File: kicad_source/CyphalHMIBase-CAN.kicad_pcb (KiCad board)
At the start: 2 copper layers, 52 x 36 mm, 62 parts, among them CN1 RASPBERRYPI_PICO, CN12 S3B-PH-SM4-TB, CN2 SM04B-SRSS-TB, CN3 SM04B-SRSS-TB, CN4 SM04B-GHS-TB, CN5 SM04B-GHS-TB, CN7 DNI, CN8 DNI, SW1 PTS636 SM43 SMTR LFS, U3 M24C64-RMN6TP, U8 MCP2515T-I/SO, U9 SN65HVD230, Y1 X322516MLB4SI

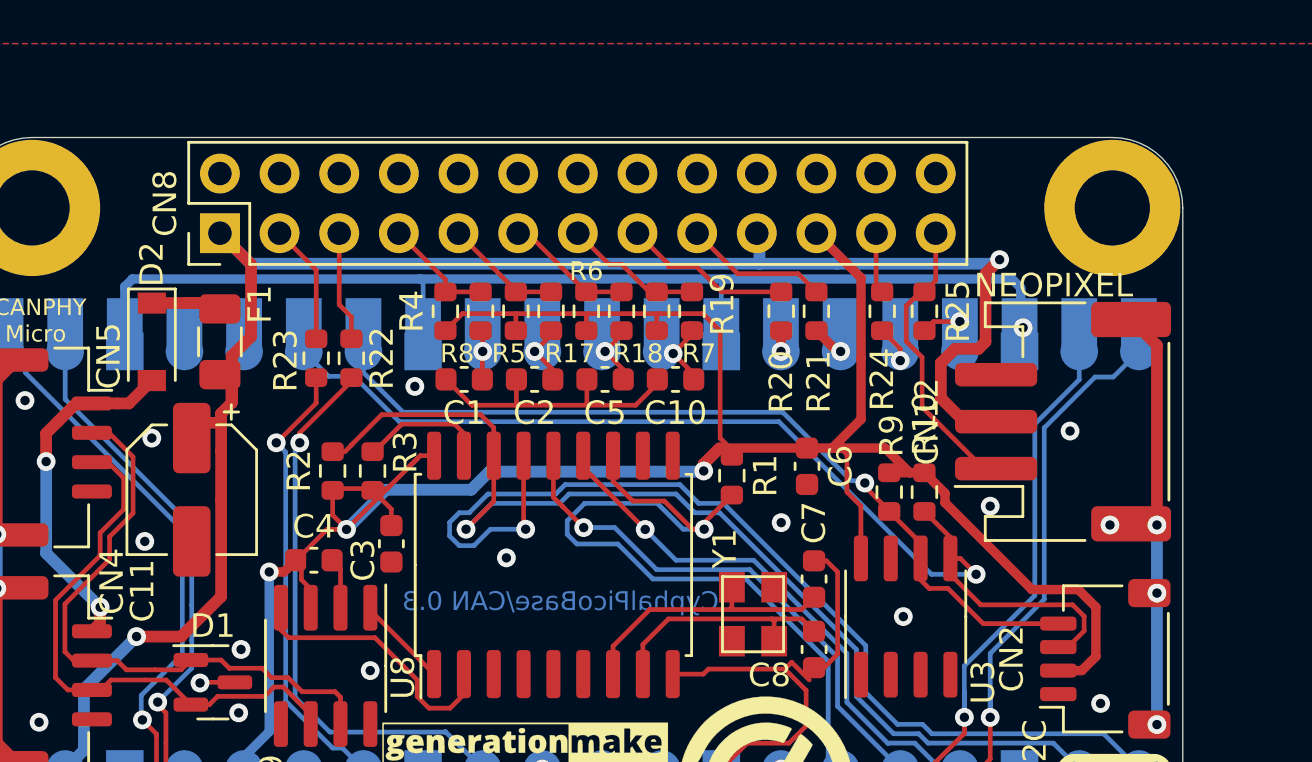
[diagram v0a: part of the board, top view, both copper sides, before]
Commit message: removed unnecessary parts
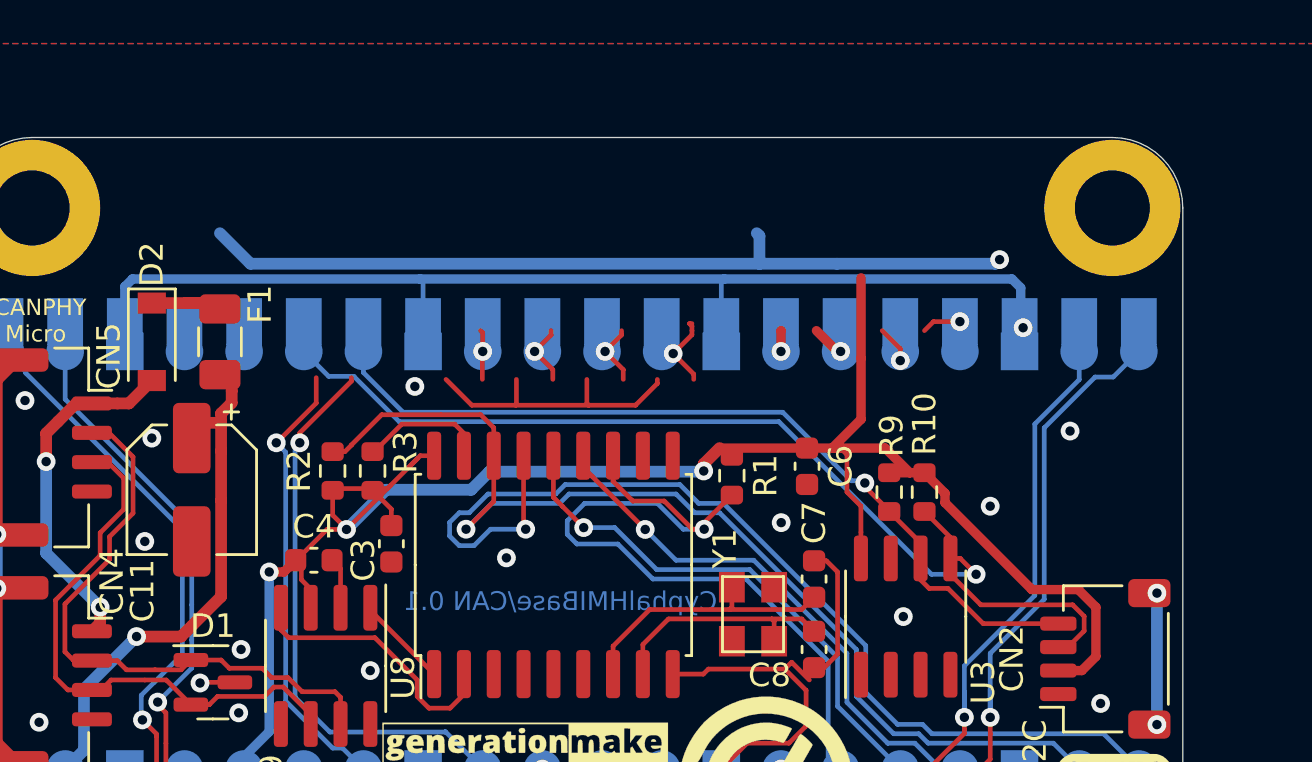
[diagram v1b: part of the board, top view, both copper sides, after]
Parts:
- removed C1, C10, C2, C5: 100nF, Capacitor_SMD:C_0603_1608Metric
- removed CN12: S3B-PH-SM4-TB, generationmake:JST_PH_S3B-PH-SM4-TB_1x03-1MP_P2.00mm_Horizontal
- removed CN8: DNI, Connector_PinHeader_2.54mm:PinHeader_2x13_P2.54mm_Vertical
- removed R17, R18, R19, R4, R5, R6, R7, R8: 10k, Resistor_SMD:R_0603_1608Metric
- removed R20, R21, R22, R23, R24, R25: 100R, Resistor_SMD:R_0603_1608Metric
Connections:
- CN1 pad 10: /INPUT1 -> /TFT_DC
- CN1 pad 11: /INPUT2 -> unconnected-(CN1-GP8/SPI1_RX/I2C0_SDA/UART1_TX-Pad11)
- CN1 pad 12: /INPUT3 -> /TFT_RST
- CN1 pad 14: /OUTPUT0 -> /SPI1_CLK
- CN1 pad 15: /OUTPUT1 -> /SPI1_MOSI
- CN1 pad 16: /RESERVED0 -> /SPI1_MISO
- CN1 pad 17: /NEOPIXEL -> /ROT_SW
- CN1 pad 32: /ANALOG_INPUT0 -> /ROT_A
- CN1 pad 34: /ANALOG_INPUT1 -> /ROT_B
- CN1 pad 9: /INPUT0 -> /TFT_CS
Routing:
- net /ROT_A: track 0.00 -> 25.1 mm, vias 0 -> 1
- net /ANALOG_INPUT0: track 25.1 -> 0.00 mm, vias 1 -> 0
- net +3V3: track 113.3 -> 90.8 mm
- net /ROT_B: track 0.00 -> 20.4 mm, vias 0 -> 1
- net /ANALOG_INPUT1: track 20.4 -> 0.00 mm, vias 1 -> 0
- net +BATT: track 120.7 -> 102.3 mm
- net /MP2: track 19.7 -> 5.60 mm, vias 4 -> 2
- net /NEOPIXEL_R: track 12.6 -> 0.00 mm
- net (no net): track 0.00 -> 9.04 mm, vias 0 -> 1
- net /OUTPUT0_R: track 7.22 -> 0.00 mm
- net /OUTPUT1_R: track 6.12 -> 0.00 mm
- net /INPUT3_R: track 5.90 -> 0.00 mm
- net /INPUT2_R: track 5.44 -> 0.00 mm
- net /ANALOG_INPUT1_R: track 5.15 -> 0.00 mm
- net /INPUT1_R: track 5.01 -> 0.00 mm
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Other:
- board text added: "CyphalHMIBase/CAN 0.1"
- board text added: "find data and documentation at https://github.com/generationmake/CyphalHMIBase-CAN"
- board text removed: "+3V3"
- board text removed: "ANALOG0"
- board text removed: "ANALOG1"
- board text removed: "CyphalPicoBase/CAN 0.3"
- board text removed: "INPUT0"
- board text removed: "INPUT1"
- board text removed: "INPUT2"
- board text removed: "INPUT3"
- board text removed: "NEOPIXEL"
- board text removed: "OUTPUT0"
- board text removed: "OUTPUT1"
- board text removed: "RESERVED0"
- board text removed: "V_IN"
- board text removed: "find data and documentation at https://github.com/generationmake/CyphalPicoBase-CAN"
